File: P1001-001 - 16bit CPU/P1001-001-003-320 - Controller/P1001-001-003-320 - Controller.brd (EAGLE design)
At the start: 200 x 152 mm, 149 parts, among them IC1 74ALS00D, IC10 74ALS04D, IC11 74ALS04D, IC2 74ALS02D, IC21 74LS138D, IC22 74LS138D, IC27 MEGA8535-A, IC6 74ALS08D, IC8 74ALS04D, IC9 74ALS04D

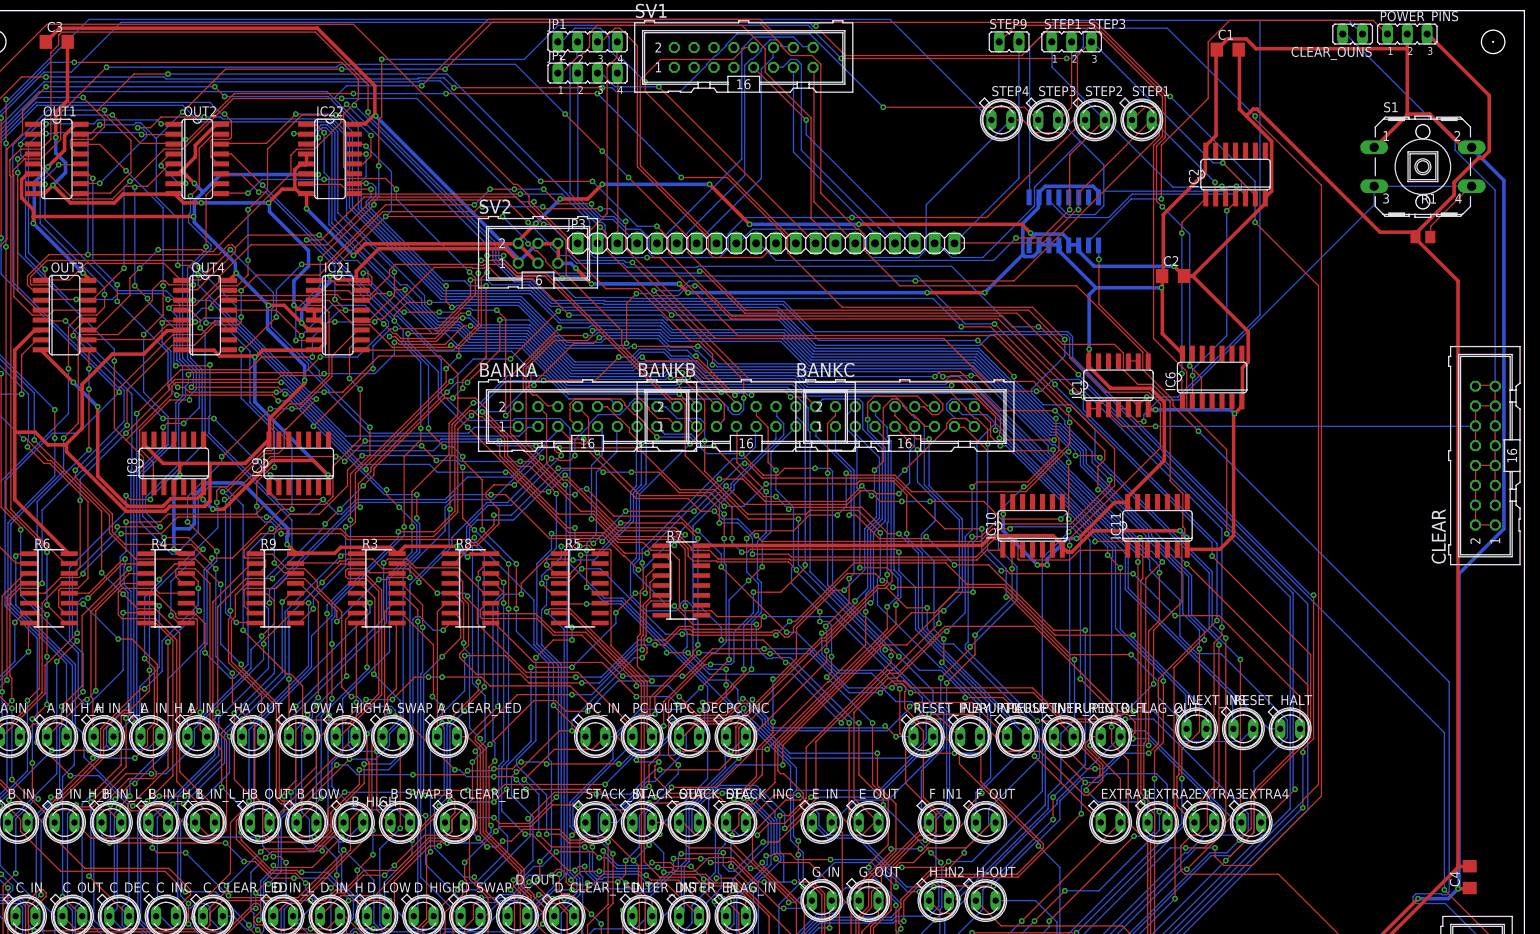
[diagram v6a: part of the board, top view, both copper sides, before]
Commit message: add ram to Memory
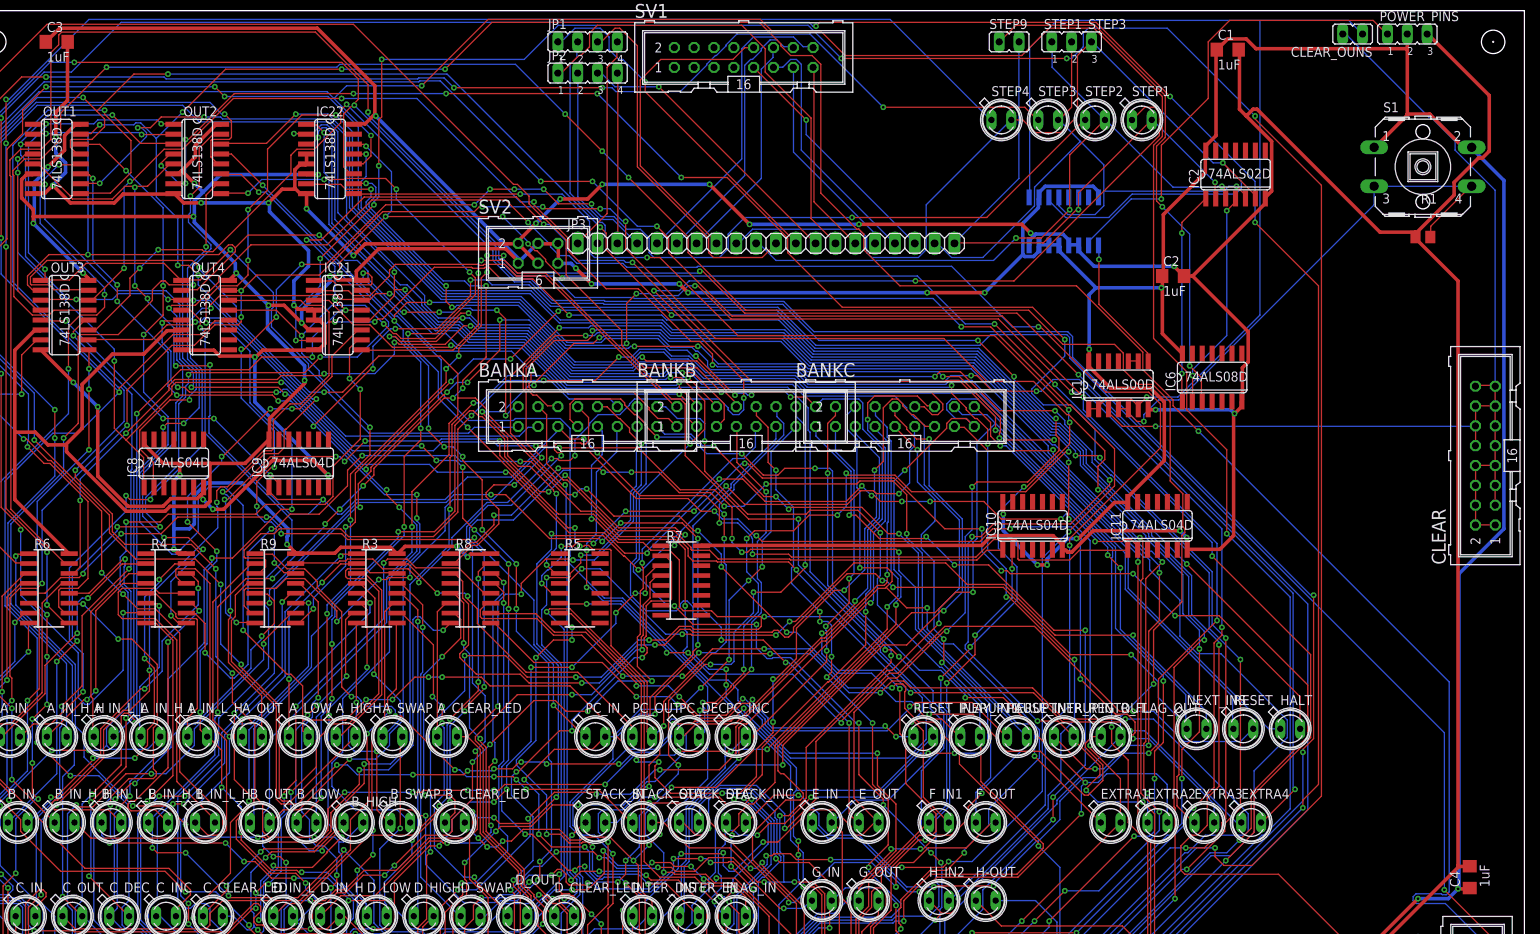
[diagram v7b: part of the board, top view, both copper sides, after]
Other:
- board text added: "Copyright 2020 James Wright"
- board text added: "P1001-001-003-320 - Controller"
